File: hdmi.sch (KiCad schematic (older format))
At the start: 31 parts, among them J1901 Mini-HDMI, Q1901 NX3020NAKS, Q1902 NX3020NAKS, Q1903 NX3020NAKS, Q1904 NX3020NAKS, U1901 PCMF3HDMI2SZ, U1902 PCMF2HDMI2SZ

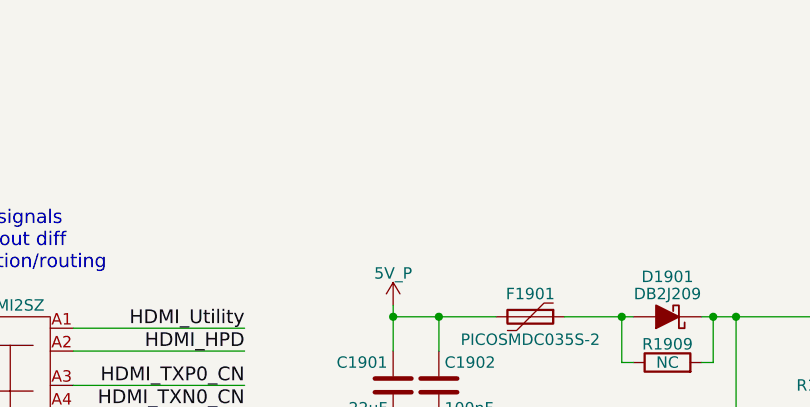
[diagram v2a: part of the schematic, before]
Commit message: Move more symbols, sheets, and pins around on the front sheet to make it even clearer, bring back the old hierarchical structure (again), bring back each sheet's title, add large text "titles" to each sheet reflecting what they are for
Still need to double check everything on the first page.
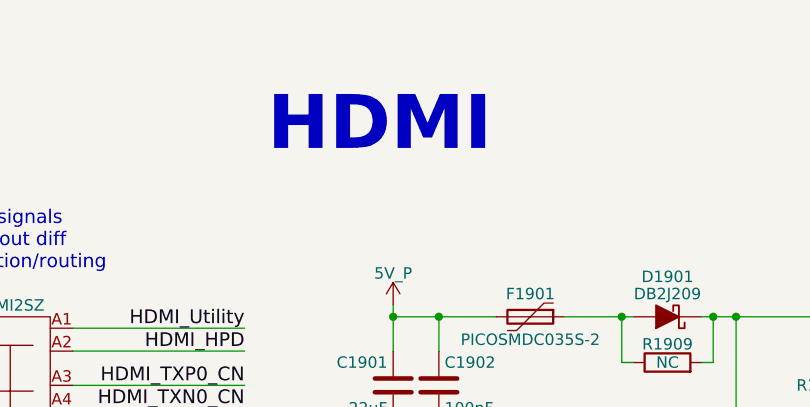
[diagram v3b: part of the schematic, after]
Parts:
- renumbered Q1902 to Q1901, Q1903 to Q1902, Q1904 to Q1902, Q1901 to Q1903, Q1902 to Q1903, Q1903 to Q1904
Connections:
- net 1V8_P: now also Q1901.5 (G), Q1902.5 (G), Q1903.2 (G), Q1904.2 (G); no longer Q1901.2 (G), Q1902.2 (G), Q1903.5 (G), Q1904.5 (G)
- net GND: now also Q1901.4 (S), Q1902.4 (S), Q1903.1 (S), Q1904.1 (S); no longer Q1901.1 (S), Q1902.1 (S), Q1903.4 (S), Q1904.4 (S)
- net at R1903.2: now also Q1901.3 (D); no longer Q1903.3 (D)
- net at R1905.2: now also Q1902.6 (D); no longer Q1901.6 (D)
- net at R1907.2: now also Q1902.3 (D); no longer Q1903.3 (D)
- net at R1902.2: now also Q1903.6 (D); no longer Q1902.6 (D)
- net at R1904.2: now also Q1903.3 (D); no longer Q1904.3 (D)
- net at R1906.2: now also Q1904.6 (D); no longer Q1902.6 (D)
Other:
- note added: "HDMI"
- moved on the sheet: Q1902A, Q1903B
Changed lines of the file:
@@
 encoding utf-8
 Sheet 19 24
-Title "Librem5 development kit"
+Title "HDMI"
 Date "2018-06-11"
 Rev "v0.1.0"
@@
 $EndComp
 $Comp
-L 1V8_P #PWR0218
+L 1V8_P #PWR0329
 U 1 1 5B01672B
 P 750 3350
-F 0 "#PWR0218" H 750 3200 50  0001 C CNN
+F 0 "#PWR0329" H 750 3200 50  0001 C CNN
 F 1 "1V8_P" H 750 3490 50  0000 C CNN
 F 2 "" H 750 3350 50  0001 C CNN
@@
 $EndComp
 $Comp
-L 1V8_P #PWR0219
+L 1V8_P #PWR0330
 U 1 1 5B019D66
 P 750 5050
-F 0 "#PWR0219" H 750 4900 50  0001 C CNN
+F 0 "#PWR0330" H 750 4900 50  0001 C CNN
 F 1 "1V8_P" H 750 5190 50  0000 C CNN
 F 2 "" H 750 5050 50  0001 C CNN
@@
 ±1%!!!
 $Comp
-L GND #PWR0220
+L GND #PWR0331
 U 1 1 5B081BE1
 P 4150 3400
-F 0 "#PWR0220" H 4150 3150 50  0001 C CNN
+F 0 "#PWR0331" H 4150 3150 50  0001 C CNN
 F 1 "GND" H 4150 3250 50  0000 C CNN
 F 2 "" H 4150 3400 50  0001 C CNN
@@
 HDMI_TXN1
 $Comp
-L GND #PWR0221
+L GND #PWR0332
 U 1 1 5B08911B
 P 4150 5100
-F 0 "#PWR0221" H 4150 4850 50  0001 C CNN
+F 0 "#PWR0332" H 4150 4850 50  0001 C CNN
 F 1 "GND" H 4150 4950 50  0000 C CNN
 F 2 "" H 4150 5100 50  0001 C CNN
@@
 Layout Note:\nMay need swap some signals\ndue to micro-HDMI pinout diff\ndepending on pin location/routing
 $Comp
-L GND #PWR0222
+L GND #PWR0333
 U 1 1 5AF69B9C
 P 9200 4900
-F 0 "#PWR0222" H 9200 4650 50  0001 C CNN
+F 0 "#PWR0333" H 9200 4650 50  0001 C CNN
 F 1 "GND" H 9200 4750 50  0000 C CNN
 F 2 "" H 9200 4900 50  0001 C CNN
@@
 $EndComp
 $Comp
-L GND #PWR0223
+L GND #PWR0334
 U 1 1 5AFABCE1
 P 6150 2400
-F 0 "#PWR0223" H 6150 2150 50  0001 C CNN
+F 0 "#PWR0334" H 6150 2150 50  0001 C CNN
 F 1 "GND" H 6150 2250 50  0000 C CNN
 F 2 "" H 6150 2400 50  0001 C CNN
@@
 $EndComp
 $Comp
-L 3V3_P #PWR0224
+L 3V3_P #PWR0335
 U 1 1 5AFBD440
 P 9200 1650
-F 0 "#PWR0224" H 9200 1500 50  0001 C CNN
+F 0 "#PWR0335" H 9200 1500 50  0001 C CNN
 F 1 "3V3_P" H 9200 1790 50  0000 C CNN
 F 2 "" H 9200 1650 50  0001 C CNN
@@
 $EndComp
 $Comp
-L 5V_P #PWR0225
+L 5V_P #PWR0336
 U 1 1 5B3E4E0C
 P 6050 1800
-F 0 "#PWR0225" H 6050 1650 50  0001 C CNN
+F 0 "#PWR0336" H 6050 1650 50  0001 C CNN
 F 1 "5V_P" H 6050 1940 50  0000 C CNN
 F 2 "" H 6050 1800 50  0001 C CNN
@@
 $EndComp
 $Comp
+L Q_NMOS_DUAL Q1903
+U 1 1 5B1A7CAB
+P 1150 4800
+F 0 "Q1903" H 800 5000 50  0000 L CNN
+F 1 "NX3020NAKS" H 600 4900 50  0000 L CNN
+F 2 "dvk-mx8m-bsb:6-TSSOP" H 1350 4900 50  0001 C CNN
+F 3 "https://assets.nexperia.com/documents/data-sheet/NX3020NAKS.pdf" H 1150 4800 50  0001 C CNN
+F 4 "NXP" H 1150 4800 60  0001 C CNN "MFG Name"
+F 5 "NX3020NAKS" H 1150 4800 60  0001 C CNN "MFG Part Num"
+F 6 "NX3020NAKS,115" H 1150 4800 60  0001 C CNN "Distrib PN"
+F 7 "https://www.arrow.com/en/products/nx3020naks115/nexperia" H 1150 4800 60  0001 C CNN "Distrib Link"
+F 8 "-" H 1150 4800 60  0001 C CNN "Tolerance"
+F 9 "https://octopart.com/search?q=NX3020NAKS&start=0" H 1150 4800 60  0001 C CNN "Others"
+	1    1150 4800
+	1    0    0    -1
+$EndComp
+$Comp
 L Q_NMOS_DUAL Q1901
-U 2 1 5B1A7CAB
+U 2 1 5B1A8769
 P 1900 3100
 F 0 "Q1901" H 1550 3300 50  0000 L CNN
@@
 $Comp
 L Q_NMOS_DUAL Q1902
-U 1 1 5B1A8769
+U 1 1 5B1A87F5
 P 2650 3100
 F 0 "Q1902" H 2300 3300 50  0000 L CNN
@@
 $EndComp
 $Comp
+L Q_NMOS_DUAL Q1902
+U 2 1 5B1A8AD3
+P 3400 3100
+F 0 "Q1902" H 3050 3300 50  0000 L CNN
+F 1 "NX3020NAKS" H 2850 3200 50  0000 L CNN
+F 2 "dvk-mx8m-bsb:6-TSSOP" H 3600 3200 50  0001 C CNN
+F 3 "https://assets.nexperia.com/documents/data-sheet/NX3020NAKS.pdf" H 3400 3100 50  0001 C CNN
+F 4 "NXP" H 3400 3100 60  0001 C CNN "MFG Name"
+F 5 "NX3020NAKS" H 3400 3100 60  0001 C CNN "MFG Part Num"
+F 6 "NX3020NAKS,115" H 3400 3100 60  0001 C CNN "Distrib PN"
+F 7 "https://www.arrow.com/en/products/nx3020naks115/nexperia" H 3400 3100 60  0001 C CNN "Distrib Link"
+F 8 "-" H 3400 3100 60  0001 C CNN "Tolerance"
+F 9 "https://octopart.com/search?q=NX3020NAKS&start=0" H 3400 3100 60  0001 C CNN "Others"
+	2    3400 3100
+	1    0    0    -1
+$EndComp
+$Comp
 L Q_NMOS_DUAL Q1903
-U 1 1 5B1A87F5
-P 1150 4800
-F 0 "Q1903" H 800 5000 50  0000 L CNN
-F 1 "NX3020NAKS" H 600 4900 50  0000 L CNN
-F 2 "dvk-mx8m-bsb:6-TSSOP" H 1350 4900 50  0001 C CNN
-F 3 "https://assets.nexperia.com/documents/data-sheet/NX3020NAKS.pdf" H 1150 4800 50  0001 C CNN
-F 4 "NXP" H 1150 4800 60  0001 C CNN "MFG Name"
-F 5 "NX3020NAKS" H 1150 4800 60  0001 C CNN "MFG Part Num"
-F 6 "NX3020NAKS,115" H 1150 4800 60  0001 C CNN "Distrib PN"
-F 7 "https://www.arrow.com/en/products/nx3020naks115/nexperia" H 1150 4800 60  0001 C CNN "Distrib Link"
-F 8 "-" H 1150 4800 60  0001 C CNN "Tolerance"
-F 9 "https://octopart.com/search?q=NX3020NAKS&start=0" H 1150 4800 60  0001 C CNN "Others"
-	1    1150 4800
+U 2 1 5B1A9D21
+P 1900 4800
+F 0 "Q1903" H 1550 5000 50  0000 L CNN
+F 1 "NX3020NAKS" H 1350 4900 50  0000 L CNN
+F 2 "dvk-mx8m-bsb:6-TSSOP" H 2100 4900 50  0001 C CNN
+F 3 "https://assets.nexperia.com/documents/data-sheet/NX3020NAKS.pdf" H 1900 4800 50  0001 C CNN
+F 4 "NXP" H 1900 4800 60  0001 C CNN "MFG Name"
+F 5 "NX3020NAKS" H 1900 4800 60  0001 C CNN "MFG Part Num"
+F 6 "NX3020NAKS,115" H 1900 4800 60  0001 C CNN "Distrib PN"
+F 7 "https://www.arrow.com/en/products/nx3020naks115/nexperia" H 1900 4800 60  0001 C CNN "Distrib Link"
+F 8 "-" H 1900 4800 60  0001 C CNN "Tolerance"
+F 9 "https://octopart.com/search?q=NX3020NAKS&start=0" H 1900 4800 60  0001 C CNN "Others"
+	2    1900 4800
 	1    0    0    -1
 $EndComp
 $Comp
 L Q_NMOS_DUAL Q1904
-U 1 1 5B1A8AD3
+U 1 1 5B1A9DC4
 P 2650 4800
 F 0 "Q1904" H 2300 5000 50  0000 L CNN
@@
 F 9 "https://octopart.com/search?q=NX3020NAKS&start=0" H 2650 4800 60  0001 C CNN "Others"
 	1    2650 4800
-	1    0    0    -1
-$EndComp
-$Comp
-L Q_NMOS_DUAL Q1902
-U 2 1 5B1A9D21
-P 3400 3100
-F 0 "Q1902" H 3050 3300 50  0000 L CNN
-F 1 "NX3020NAKS" H 2850 3200 50  0000 L CNN
-F 2 "dvk-mx8m-bsb:6-TSSOP" H 3600 3200 50  0001 C CNN
-F 3 "https://assets.nexperia.com/documents/data-sheet/NX3020NAKS.pdf" H 3400 3100 50  0001 C CNN
-F 4 "NXP" H 3400 3100 60  0001 C CNN "MFG Name"
-F 5 "NX3020NAKS" H 3400 3100 60  0001 C CNN "MFG Part Num"
-F 6 "NX3020NAKS,115" H 3400 3100 60  0001 C CNN "Distrib PN"
-F 7 "https://www.arrow.com/en/products/nx3020naks115/nexperia" H 3400 3100 60  0001 C CNN "Distrib Link"
-F 8 "-" H 3400 3100 60  0001 C CNN "Tolerance"
-F 9 "https://octopart.com/search?q=NX3020NAKS&start=0" H 3400 3100 60  0001 C CNN "Others"
-	2    3400 3100
-	1    0    0    -1
-$EndComp
-$Comp
-L Q_NMOS_DUAL Q1903
-U 2 1 5B1A9DC4
-P 1900 4800
-F 0 "Q1903" H 1550 5000 50  0000 L CNN
-F 1 "NX3020NAKS" H 1350 4900 50  0000 L CNN
-F 2 "dvk-mx8m-bsb:6-TSSOP" H 2100 4900 50  0001 C CNN
-F 3 "https://assets.nexperia.com/documents/data-sheet/NX3020NAKS.pdf" H 1900 4800 50  0001 C CNN
-F 4 "NXP" H 1900 4800 60  0001 C CNN "MFG Name"
-F 5 "NX3020NAKS" H 1900 4800 60  0001 C CNN "MFG Part Num"
-F 6 "NX3020NAKS,115" H 1900 4800 60  0001 C CNN "Distrib PN"
-F 7 "https://www.arrow.com/en/products/nx3020naks115/nexperia" H 1900 4800 60  0001 C CNN "Distrib Link"
-F 8 "-" H 1900 4800 60  0001 C CNN "Tolerance"
-F 9 "https://octopart.com/search?q=NX3020NAKS&start=0" H 1900 4800 60  0001 C CNN "Others"
-	2    1900 4800
 	1    0    0    -1
 $EndComp
@@
 Connection ~ 8650 3800
 Connection ~ 9200 3600
+Text Notes 5500 1150 0    236  ~ 47
+HDMI
 $EndSCHEMATC

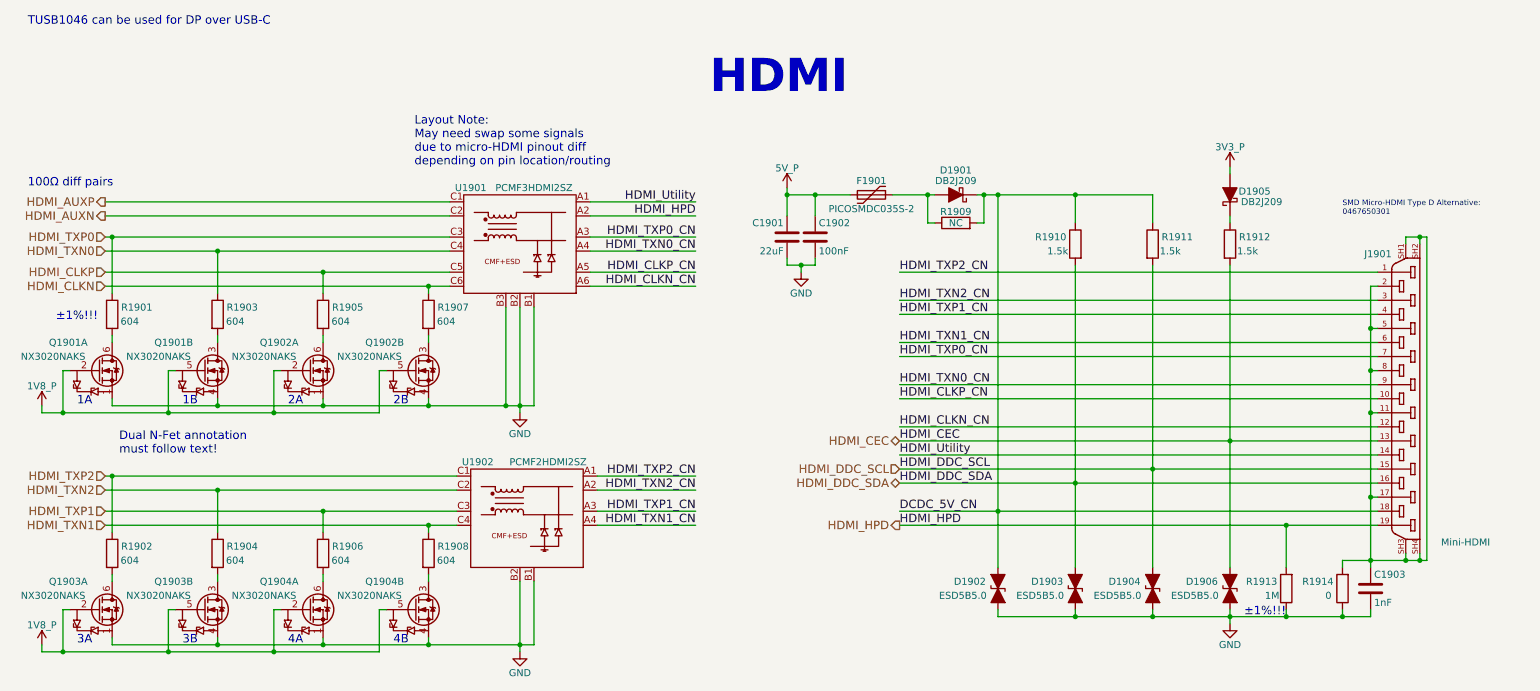
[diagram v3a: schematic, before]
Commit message: Make all differential pair signal names end in P/N so that diff routing works when in layout
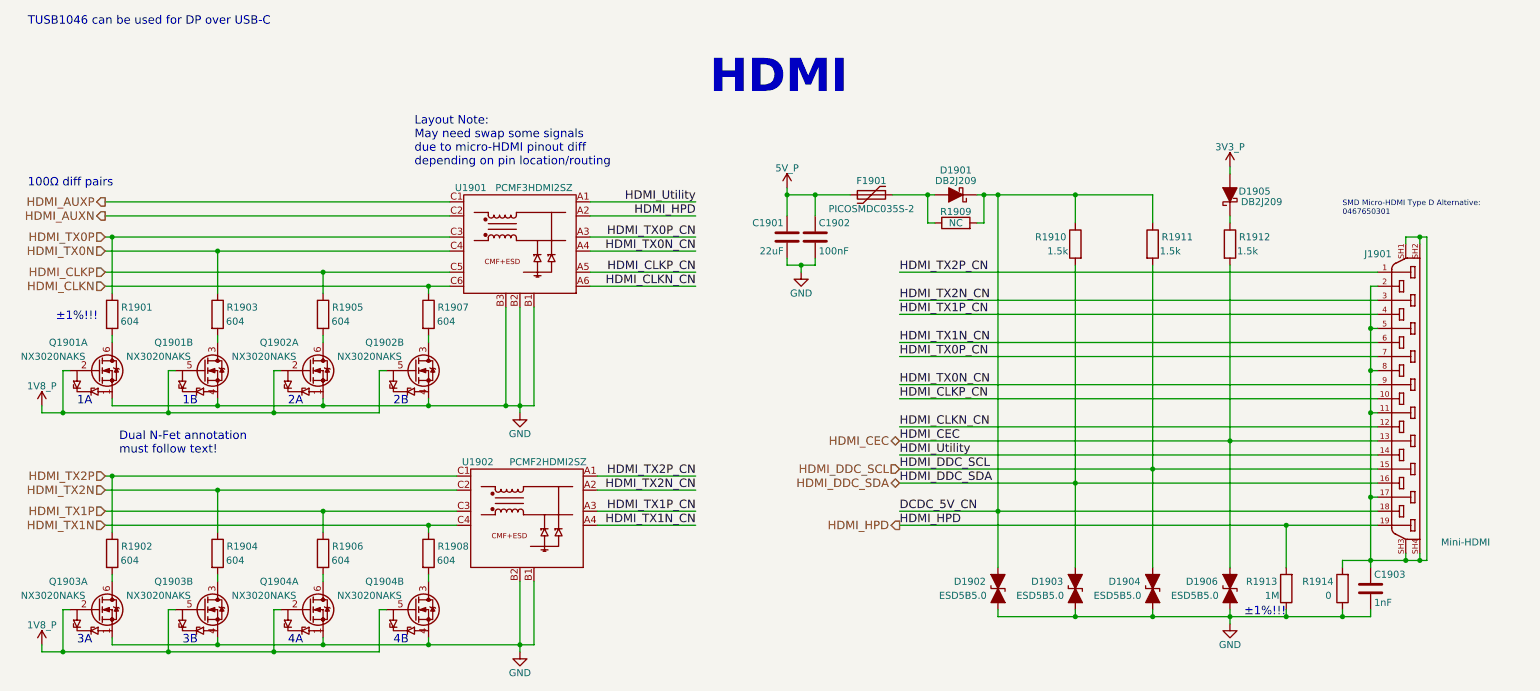
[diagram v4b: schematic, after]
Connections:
- net HDMI_TXN0 renamed HDMI_TX0N
- net HDMI_TXN0_CN renamed HDMI_TX0N_CN
- net HDMI_TXN1 renamed HDMI_TX1N
- net HDMI_TXN1_CN renamed HDMI_TX1N_CN
- net HDMI_TXN2 renamed HDMI_TX2N
- net HDMI_TXN2_CN renamed HDMI_TX2N_CN
- net HDMI_TXP0 renamed HDMI_TX0P
- net HDMI_TXP0_CN renamed HDMI_TX0P_CN
- net HDMI_TXP1 renamed HDMI_TX1P
- net HDMI_TXP1_CN renamed HDMI_TX1P_CN
- net HDMI_TXP2 renamed HDMI_TX2P
- net HDMI_TXP2_CN renamed HDMI_TX2P_CN
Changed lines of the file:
@@
 HDMI_AUXN
 Text HLabel 1200 2150 0    60   Input ~ 0
-HDMI_TXP0
+HDMI_TX0P
 Text HLabel 1200 2250 0    60   Input ~ 0
-HDMI_TXN0
+HDMI_TX0N
 Text HLabel 1200 2400 0    60   Input ~ 0
 HDMI_CLKP
@@
 HDMI_CLKN
 Text HLabel 1200 3850 0    60   Input ~ 0
-HDMI_TXP2
+HDMI_TX2P
 Text HLabel 1200 3950 0    60   Input ~ 0
-HDMI_TXN2
+HDMI_TX2N
 Text HLabel 1200 4100 0    60   Input ~ 0
-HDMI_TXP1
+HDMI_TX1P
 Text HLabel 1200 4200 0    60   Input ~ 0
-HDMI_TXN1
+HDMI_TX1N
 $Comp
 L GND #PWR0332
@@
 HDMI_Utility
 Text Label 6850 2400 0    60   ~ 0
-HDMI_TXP2_CN
+HDMI_TX2P_CN
 Text Label 6850 2600 0    60   ~ 0
-HDMI_TXN2_CN
+HDMI_TX2N_CN
 Text Label 6850 2700 0    60   ~ 0
-HDMI_TXP1_CN
+HDMI_TX1P_CN
 Text Label 6850 2900 0    60   ~ 0
-HDMI_TXN1_CN
+HDMI_TX1N_CN
 Text Label 6850 3000 0    60   ~ 0
-HDMI_TXP0_CN
+HDMI_TX0P_CN
 Text Label 6850 3200 0    60   ~ 0
-HDMI_TXN0_CN
+HDMI_TX0N_CN
 Text Label 6850 3300 0    60   ~ 0
 HDMI_CLKP_CN
@@
 HDMI_HPD
 Text Label 5400 2150 2    60   ~ 0
-HDMI_TXP0_CN
+HDMI_TX0P_CN
 Text Label 5400 2250 2    60   ~ 0
-HDMI_TXN0_CN
+HDMI_TX0N_CN
 Text Label 5400 2400 2    60   ~ 0
 HDMI_CLKP_CN
@@
 HDMI_CLKN_CN
 Text Label 5400 3850 2    60   ~ 0
-HDMI_TXP2_CN
+HDMI_TX2P_CN
 Text Label 5400 3950 2    60   ~ 0
-HDMI_TXN2_CN
+HDMI_TX2N_CN
 Text Label 5400 4100 2    60   ~ 0
-HDMI_TXP1_CN
+HDMI_TX1P_CN
 Text Label 5400 4200 2    60   ~ 0
-HDMI_TXN1_CN
+HDMI_TX1N_CN
 Text Notes 10000 2000 0    39   ~ 0
 SMD Micro-HDMI Type D Alternative:\n0467650301

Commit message: Reorder USB-C's diff pairs based on layout simplicity as done on EmCraft's Rev 2 baseboard (requires Lane Polarity Inversion), add 2 and 3-channel differential filter & TVS IC footprints (used with USB-C and HDMI), import USB-C receptacle 3D model
Used a scaled version BGA-256_16x16_17.0x17.0mm_Pitch1.0mm 3D model for the filter&TVS diff pair chips, the perimeter balls are not very noticable at this shrunken scale and can be replaced later on (placeholder).
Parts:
- U1901: footprint (none) -> dvk-mx8m-bsb:PCMF3HDMI2S
- U1902: footprint (none) -> dvk-mx8m-bsb:PCMF2HDMI2S
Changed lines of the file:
@@
 F 0 "U1901" H 3800 2600 50  0000 C CNN
 F 1 "PCMF3HDMI2SZ" H 4250 2600 50  0000 C CNN
-F 2 "" V 4025 2285 50  0001 C CNN
-F 3 "" V 4025 2285 50  0000 C CNN
+F 2 "dvk-mx8m-bsb:PCMF3HDMI2S" V 4025 2285 50  0001 C CNN
+F 3 "https://assets.nexperia.com/documents/data-sheet/PCMFXHDMI2S_SER.pdf" H 4025 2285 50  0001 C CNN
 	1    4150 2200
 	1    0    0    -1
@@
 F 0 "U1902" H 3850 4550 50  0000 C CNN
 F 1 "PCMF2HDMI2SZ" H 4350 4550 50  0000 C CNN
-F 2 "" V 4075 4235 50  0001 C CNN
-F 3 "" V 4075 4235 50  0000 C CNN
+F 2 "dvk-mx8m-bsb:PCMF2HDMI2S" V 4075 4235 50  0001 C CNN
+F 3 "https://assets.nexperia.com/documents/data-sheet/PCMFXHDMI2S_SER.pdf" H 4075 4235 50  0001 C CNN
 	1    4200 4150
 	1    0    0    -1
